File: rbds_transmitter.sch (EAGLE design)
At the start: 111 parts, among them IC1 MAX1551, IC2 TPS61030, IC3 MCP4812, IC4 OPA4743UA, IC5 OPA4743UA, IC6 MAX2606, Q1 P-Ch, Q2 P-CH, SW1 FSMSM, U3 ATMEGA328, X1 HD44780LCD-1602, Y1 16Mhz

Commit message: rebuilding filter systems
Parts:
- removed C13: 3.8nF, adafruit:C-USC1206
- removed C15, C16, C17, C20, C21, C22, C26, C27, C35, C36, C37: (no value), adafruit:C-USC1206
- removed IC4, IC5: OPA4743UA, linear:OPA4743UA
- removed R22, R23, R24, R28, R29, R30, R31, R32, R33, R34, R35, R37, R40, R41: (no value), adafruit:R-US_R1206
- removed R26, R27, R36: 100k, rcl:R-TRIMM4G/J
- added C33, C38, C39, C40, C41, C42, C43, C45, C46, C47, C48, C49, C50, C51, C52, C53, C54, C55, C56, C57: (no value), adafruit:C-USC1206
- added IC11, IC12: OPA4743UA, linear:OPA4743UA
- added R46, R47, R48, R49, R50, R52, R53, R54, R56, R57, R58, R61, R62, R63, R64, R65, R66, R68, R69, R70, R71: (no value), adafruit:R-US_R1206
- added R51, R55, R59, R67: 100k, rcl:R-TRIMM4G/J
- C11: value 10uF -> (none)
- C12: value 1.9nF -> (none)
- R16, R17: value 100k -> (none)
- R18, R19: value 1k -> 100k; device adafruit:R-US_R1206 -> rcl:R-TRIMM4G/J
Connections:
- removed net N$21: C27.2
- removed net N$25: C13.1, R18.1, R19.2
- removed net N$31: C12.1, IC4A.+IN, R19.1
- removed net N$32: C17.1, R26.S
- removed net N$34: C15.1, IC4D.+IN, R28.1
- removed net N$36: C16.1, R28.2, R29.1
- removed net N$37: C21.1, R36.S
- removed net N$38: C17.2, R29.2, R30.1, R31.2
- removed net N$40: C20.1, IC5A.+IN, R35.2
- removed net N$41: C22.1, R34.2, R35.1
- removed net N$43: C21.2, R32.2, R33.1, R34.1
- removed net N$44: C13.2, C35.1, IC4A.-IN, IC4A.OUT
- removed net N$45: C22.2, C36.1, IC5A.-IN, IC5A.OUT
- removed net N$47: C24.1, IC5C.+IN, R39.1
- removed net N$48: C37.2, R24.2
- removed net N$49: C11.1, R27.S
- removed net N$51: C26.2, R38.2, R40.1, R41.2
- removed net N$56: C36.2, R22.2
- removed net N$57: C35.2, R23.2
- new net FREQUENCY_OFFSET: R20.1
- new net N$59: C56.1, R65.1, R66.2
- new net N$60: C38.1, R46.1, R47.2
- new net N$61: C39.1, R47.1, R48.2
- new net N$62: C40.1, R48.1, R51.A
- new net N$63: C54.1, R67.A, R71.1
- new net N$64: IC11B.-IN, R51.S
- new net N$65: C41.1, IC11B.OUT, R51.E
- new net N$66: C53.1, IC12B.+IN, R49.1, R50.2
- new net N$67: C43.1, R52.1, R53.2
- new net N$68: C45.1, R53.1, R54.2
- new net N$69: C46.1, R54.1, R55.A
- new net N$70: IC11D.-IN, R55.S
- new net N$71: C47.1, IC11D.OUT, R55.E
- new net N$72: C49.1, R56.1, R57.2
- new net N$73: C50.1, R57.1, R58.2
- new net N$74: C51.1, R58.1, R59.A
- new net N$75: IC11C.-IN, R59.S
- new net N$76: C52.1, IC11C.OUT, R59.E
- new net N$77: IC11A.-IN, R67.S
- new net N$78: C41.2, R61.2
- new net N$79: C47.2, R62.2
- new net N$80: C52.2, R63.2
- new net N$81: C11.1, R61.1, R62.1, R63.1
- new net N$82: C25.1, IC11A.OUT, R67.E
- new net N$83: C33.1, R46.2, R68.1
- new net N$84: C42.1, R52.2, R69.1
- new net N$85: C48.1, R56.2, R70.1
- new net N$86: C57.1, R66.1, R71.2
- net +5V: now also IC11P.V+, IC12P.V+, R17.1, R39.1, R50.1; no longer IC4P.V+, IC5P.V+, R16.2, R31.1, R32.1, R41.1
- net AGND: now also IC11A.+IN, IC11B.+IN, IC11C.+IN, IC11D.+IN, IC12A.+IN, IC12B.-IN, IC12B.OUT, R19.A
- net BPSK: now also C23.1, IC12C.-IN, IC12C.OUT; no longer IC4C.-IN, IC4C.OUT, R15.2
- net CARRIER: now also R64.2; no longer C26.1
- net FREQUENCY: now also IC12D.-IN, IC12D.OUT; no longer IC5B.-IN, IC5B.OUT, R37.2
- net GND: now also C33.2, C38.2, C39.2, C40.2, C42.2, C43.2, C45.2, C46.2, C48.2, C49.2, C50.2, C51.2, C53.2, C54.2, C55.2, C56.2, C57.2, IC11P.V-, IC12P.V-, R16.2, R21.2, R38.2, R49.2, TR2.3; no longer C12.2, C15.2, C20.2, C24.2, IC4P.V-, IC5D.+IN, IC5P.V-, R17.1, R20.2, R26.A, R27.A, R30.2, R33.2, R36.A, R40.2, TR1.3
- net N$19: now also TR1.3; no longer TR2.5
- net N$22: now also IC12A.-IN, R18.S; no longer C11.2, R16.1, R17.2, R18.2
- net N$23: now also IC12A.OUT, R18.E, R19.E; no longer IC4B.-IN, R20.1, R21.2
- net N$26: now also C12.1, R19.S; no longer C27.1, IC4B.OUT, R21.1
- net N$28: now also IC12C.+IN; no longer IC4C.+IN
- net N$29: now also C12.2, R20.2, R21.1; no longer C16.2, C37.1, IC4D.-IN, IC4D.OUT
- net N$30: now also R15.2; no longer C25.1, IC5C.-IN, IC5C.OUT
- net N$42: now also C24.1, TR2.5; no longer C23.1, R38.1, R39.2
- net N$46: now also IC12D.+IN; no longer IC5B.+IN
- net N$5: now also C11.2, R16.1, R17.2, R18.A; no longer IC4B.+IN, R22.1, R23.1, R24.1, R37.1
- net N$55: now also C55.1, R64.1, R65.2; no longer IC5D.-IN, IC5D.OUT
- net PILOT: now also R69.2; no longer R36.E
- net RBDS: now also C24.2, R38.1, R39.2, R68.2; no longer R27.E, TR2.3
- net TONE: now also R70.2; no longer R26.E
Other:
- moved on the sheet: ANT1, ANT2, C1, C10, C11, C12, C14, C18, C19, C2, C23, C24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

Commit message: need to wire subsystems to mcu
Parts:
- removed SW1: FSMSM, alcoswitch:FSMSM
- C1: value 4.7uF -> 1nF
- C11, C12, C14, C28, C32, C41, C47, C52, C53, C9: value (none) -> 1uF
- C18, C29, C30, C8: value (none) -> 4.7uF
- C19, C34: value (none) -> 100pF
- C23, C24, C25: value (none) -> 10uF
- C33, C38, C39, C40: value (none) -> 1.34nF
- C42, C43, C45, C46: value (none) -> 4.188nF
- C48, C49, C50, C51: value (none) -> 3.06nF
- C54, C55, C56, C57: value (none) -> 1.396nF
- C7: value (none) -> 100uF; device adafruit:C-USC1206 -> adafruit:CPOL-US140CLH-1014
- L2: value (none) -> 485nH
- R11, R16, R17, R20, R21, R38, R39, R49, R50: value (none) -> 100k
- R44, R45: value (none) -> 10k
- R46, R47, R48, R52, R53, R54, R56, R57, R58, R64, R65, R66, R68, R69, R70, R71: value (none) -> 2k
- R61, R62, R63: value (none) -> 1k
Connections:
- removed net FREQUENCY_OFFSET: R20.1
- removed net N$29: C12.2, R20.2, R21.1
- removed net N$58: R42.1
- removed net RST: C1.2
- new net SIGNAL: C12.2, R20.2, R21.1, R42.1
- net !ISP-RST: no longer C1.1, SW1.S
- net +5V: now also C7.+; no longer C7.1
- net FREQUENCY: now also R20.1
- net GND: now also C1.2, C7.-; no longer C7.2, SW1.P
- net N$27: now also C1.1
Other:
- moved on the sheet: ANT1, ANT2, C1, C10, C11, C12, C14, C18, C19, C2, C23, C24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

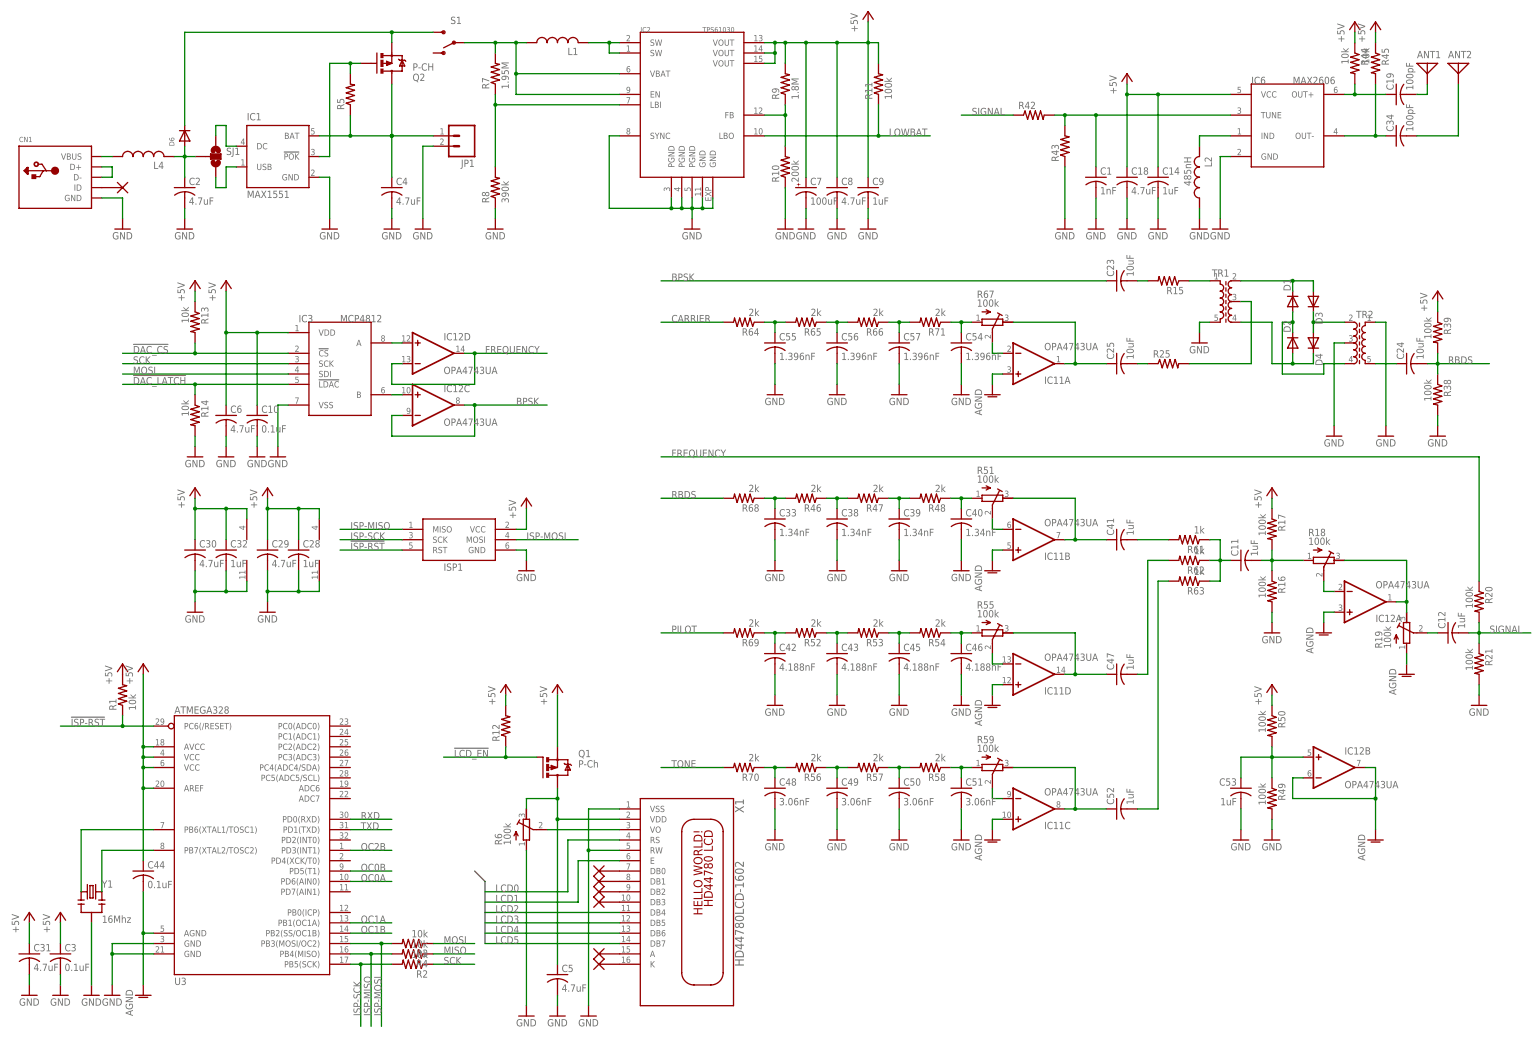
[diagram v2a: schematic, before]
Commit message: finished prelim layout
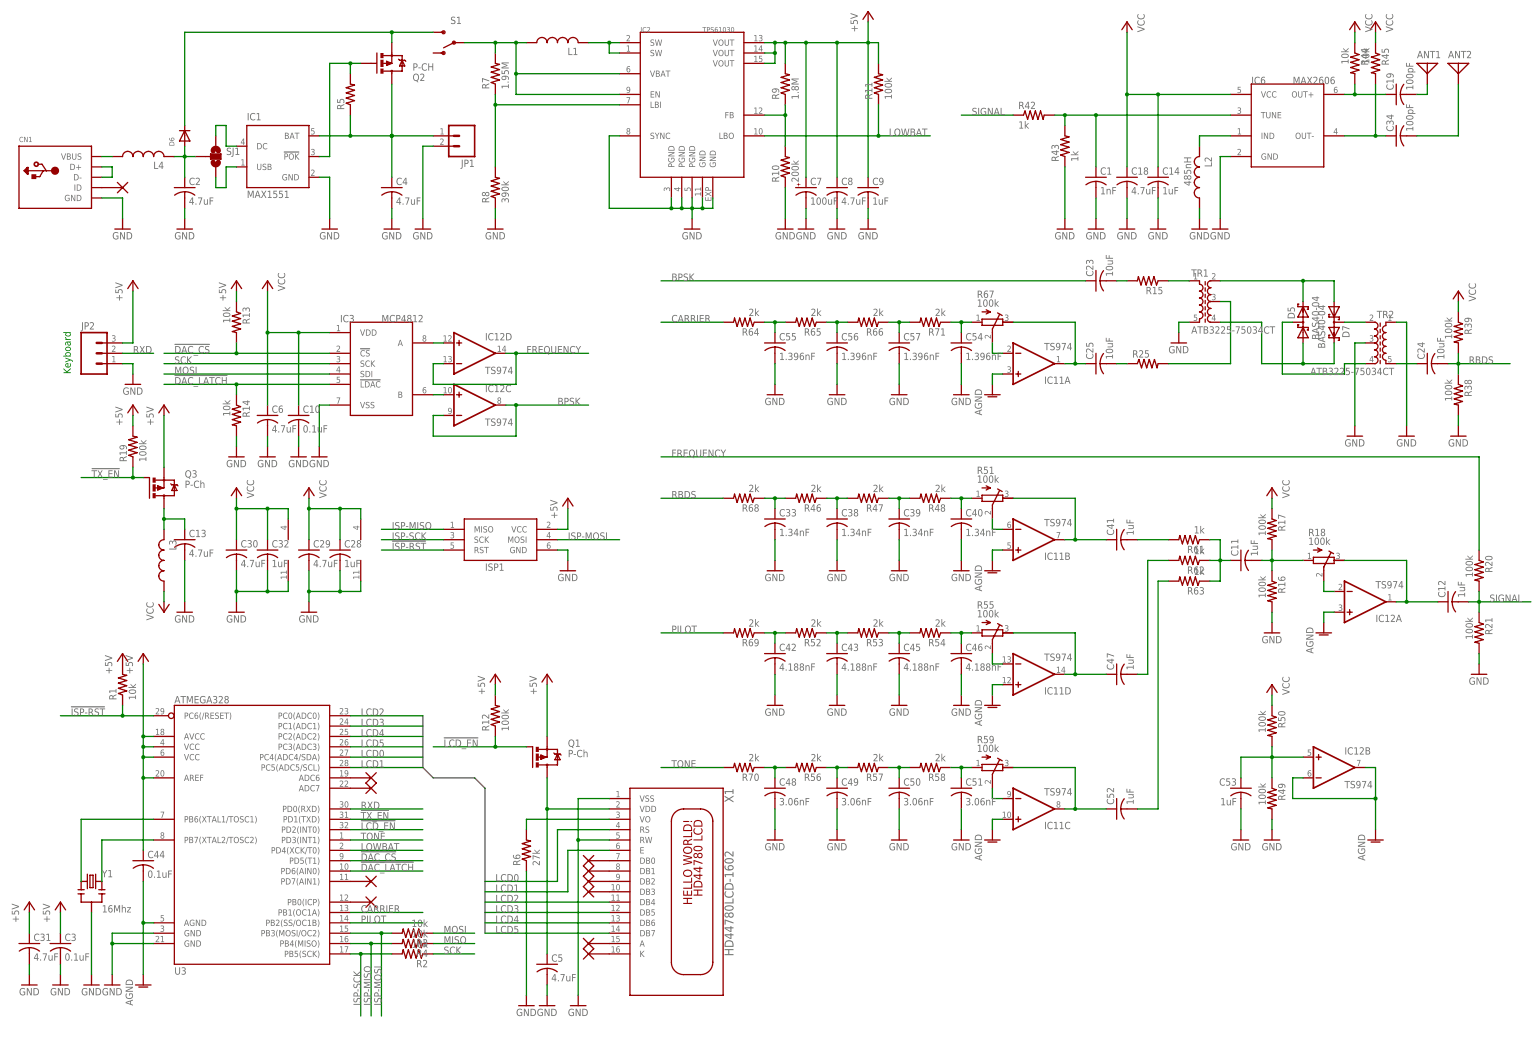
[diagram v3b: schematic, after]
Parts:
- removed D1, D2, D3, D4: (no value), dp_devices:DIODE-SOD-123
- added C13: 4.7uF, adafruit:C-USC1206
- added D5, D7: BAS40-04, diode:BAS40-04
- added JP2: (no value), sparkfun:M03PTH
- added L3: (no value), resistor:L-USL1812
- added Q3: P-Ch, transistor-power:IRLML5203
- IC11, IC12: value OPA4743UA -> TS974
- R12: value (none) -> 100k
- R19: device rcl:R-TRIMM4G/J -> adafruit:R-US_R1206
- R42, R43: value (none) -> 1k
- R6: value 100k -> 27k; device rcl:R-TRIMM4G/J -> adafruit:R-US_R1206
- TR1, TR2: value (none) -> ATB3225-75034CT
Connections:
- removed net N$26: C12.1, R19.S
- removed net OC0A: U3.PD6(AIN0)
- removed net OC0B: U3.PD5(T1)
- removed net OC1A: U3.PB1(OC1A)
- removed net OC1B: U3.PB2(SS/OC1B)
- removed net OC2B: U3.PD3(INT1)
- removed net TXD: U3.PD1(TXD)
- new net !TX_EN: Q3.G, R19.1, U3.PD1(TXD)
- new net N$21: C13.1, L3.2, Q3.D
- new net VCC: C10.1, C14.1, C18.1, C28.1, C29.1, C30.1, C32.1, C6.1, IC11P.V+, IC12P.V+, IC3.VDD, IC6.VCC, L3.1, R17.1, R39.1, R44.1, R45.1, R50.1
- net !DAC_CS: now also U3.PD5(T1)
- net !DAC_LATCH: now also U3.PD6(AIN0)
- net !LCD_EN: now also U3.PD2(INT0)
- net +5V: now also JP2.3, Q3.S, R19.2; no longer C10.1, C14.1, C18.1, C28.1, C29.1, C30.1, C32.1, C6.1, IC11P.V+, IC12P.V+, IC3.VDD, IC6.VCC, R17.1, R39.1, R44.1, R45.1, R50.1
- net AGND: no longer R19.A
- net CARRIER: now also U3.PB1(OC1A)
- net GND: now also C13.2, JP2.1, R6.1; no longer R6.A
- net LCD0: now also U3.PC4(ADC4/SDA)
- net LCD1: now also U3.PC5(ADC5/SCL)
- net LCD2: now also U3.PC0(ADC0)
- net LCD3: now also U3.PC1(ADC1)
- net LCD4: now also U3.PC2(ADC2)
- net LCD5: now also U3.PC3(ADC3)
- net LOWBAT: now also U3.PD4(XCK/T0)
- net N$14: now also D7.C1A2; no longer D3.C, D4.A
- net N$16: now also D5.C2, D7.A1; no longer D1.C, D3.A
- net N$18: now also D5.A1, D7.C2; no longer D2.A, D4.C
- net N$23: now also C12.1; no longer R19.E
- net N$3: now also D5.C1A2; no longer D1.A, D2.C
- net N$9: now also R6.2; no longer R6.S
- net PILOT: now also U3.PB2(SS/OC1B)
- net RXD: now also JP2.2
- net TONE: now also U3.PD3(INT1)
- net VDD: no longer R6.E
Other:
- note added: "Keyboard"
- moved on the sheet: C10, C12, C23, C24, C25, C28, C29, C3, C30, C31, C32, C44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

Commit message: finsihed
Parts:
- removed C47, C52, C53: 1uF, adafruit:C-USC1206
- removed C50, C51: 3.06nF, adafruit:C-USC1206
- removed C54, C55, C56, C57: 1.396nF, adafruit:C-USC1206
- removed IC11, IC12: TS974, linear:OPA4743UA
- removed R54, R56, R57, R58: 2k, adafruit:R-US_R1206
- removed R55, R59, R67: 100k, rcl:R-TRIMM4G/J
- removed R61, R62: 1k, adafruit:R-US_R1206
- added C15: 10uF, adafruit:C-USC1206
- added C16: 100pF, adafruit:C-USC1206
- added C17, C20, C21, C22, C26, C27: 4.7uF, adafruit:C-USC1206
- added C35: 1.34nF, adafruit:C-USC1206
- added IC4: MAX2606, maxim:MAX2606
- added IC5: TPS61030, texas:TPS61030
- added JP10, JP3, JP4, JP5, JP6, JP7, JP8, JP9: M01PTH, sparkfun:M01PTH
- added JP11: (no value), sparkfun:M023.5MM
- added R22, R23, R24, R40, R41: 100k, adafruit:R-US_R1206
- added R26, R27, R28: 10k, adafruit:R-US_R1206
- added R37: 1.8M, adafruit:R-US_R1206
- C10, C3: value 0.1uF -> 1uF
- C12: value 1uF -> 0.1uF
- C13: value 4.7uF -> 10uF
- C14: value 1uF -> 10uF
- C18: value 4.7uF -> 0.1uF
- C19: value 100pF -> 4.7uF
- C2, C4, C5, C6, C8: value 4.7uF -> 1uF
- C23: value 10uF -> 0.1uF
- C24, C25: value 10uF -> 4.7uF
- C28: value 1uF -> 4.7uF
- C29, C30, C31: value 4.7uF -> 1.396nF
- C32: value 1uF -> 1.34nF
- C34: value 100pF -> 1.34nF
- C38, C39: value 1.34nF -> 3.06nF
- C40: value 1.34nF -> 100pF
- C41: value 1uF -> 4.188nF
- C44: value 0.1uF -> 4.188nF
- C45: value 4.188nF -> 1.396nF
- C46: value 4.188nF -> 100uF; device adafruit:C-USC1206 -> adafruit:CPOL-US140CLH-1014
- C7: value 100uF -> 1uF; device adafruit:CPOL-US140CLH-1014 -> adafruit:C-USC1206
- IC1: value MAX1551 -> TS974; device maxim:MAX1551 -> linear:OPA4743UA
- IC2: value TPS61030 -> TS974; device texas:TPS61030 -> linear:OPA4743UA
- IC3: value MCP4812 -> MAX1551; device microchip:MCP4812 -> maxim:MAX1551
- IC6: value MAX2606 -> MCP4812; device maxim:MAX2606 -> microchip:MCP4812
- JP1: device sparkfun:M02-JST-2MM-SMT -> sparkfun:M03PTH
- JP2: device sparkfun:M03PTH -> sparkfun:M02-JST-2MM-SMT
- L2: value 485nH -> (none)
- L4: value (none) -> 485nH
- Q1: value P-Ch -> P-CH; device transistor-power:IRLML5203 -> sparkfun:MOSFET-PCHANNELSMD
- Q2: value P-CH -> P-Ch; device sparkfun:MOSFET-PCHANNELSMD -> transistor-power:IRLML5203
- R1: value 10k -> 332
- R10: value 200k -> 2k
- R11, R12, R16, R17: value 100k -> 2k
- R13, R14: value 10k -> 2k
- R15: value (none) -> 2k
- R18: value 100k -> 1k; device rcl:R-TRIMM4G/J -> adafruit:R-US_R1206
- R19: value 100k -> 1k
- R20: value 100k -> (none)
- R21: value 100k -> 200
- R25: value (none) -> 10k
- R38: value 100k -> 390k
- R39: value 100k -> 200k
- R42, R43: value 1k -> 100k
- R44, R45: value 10k -> 100k
- R46, R47: value 2k -> 100k
- R48: value 2k -> 1.95M
- R49, R50: device adafruit:R-US_R1206 -> rcl:R-TRIMM4G/J
- R5: value (none) -> 200
- R52, R53: value 2k -> 100k; device adafruit:R-US_R1206 -> rcl:R-TRIMM4G/J
- R6: value 27k -> 10k
- R7: value 1.95M -> 10k
- R8: value 390k -> 10k
- R9: value 1.8M -> 2k
- renumbered C48 to C36, C49 to C37, D5 to D2, D6 to D1, D7 to D3, R63 to R29, R64 to R30, R65 to R31, R66 to R32, R68 to R33, R69 to R34, R70 to R35, R71 to R36, S1 to SW1, U3 to U1
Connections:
- removed net N$27: C1.1, IC6.TUNE, R42.2, R43.2
- removed net N$30: C23.2, R15.2
- removed net N$53: C25.2, R25.1
- new net N$25: C13.1, R5.1
- new net N$26: C15.1, R21.2
- net !DAC_CS: now also IC6.!CS, R2.2; no longer IC3.!CS, R13.2
- net !DAC_LATCH: now also IC6.!LDAC, R3.1; no longer IC3.!LDAC, R14.1
- net !ISP-RST: now also R25.1; no longer R1.1
- net !LCD_EN: now also Q2.G, R41.1; no longer Q1.G, R12.1
- net !TX_EN: now also R44.1; no longer R19.1
- net +5V: now also C12.1, C18.1, C2.1, C22.1, C28.1, C46.+, IC5.VOUT@0, IC5.VOUT@1, IC5.VOUT@2, JP1.3, JP11.2, Q2.S, R2.1, R25.2, R37.2, R40.2, R41.2, R44.2; no longer C3.1, C31.1, C44.1, C7.+, C8.1, C9.1, IC2.VOUT@0, IC2.VOUT@1, IC2.VOUT@2, JP2.3, Q1.S, R1.2, R11.2, R12.2, R13.1, R19.2, R9.2
- net AGND: now also C12.2, IC1A.+IN, IC1B.+IN, IC1C.+IN, IC1D.+IN, IC2A.+IN, IC2B.-IN, IC2B.OUT; no longer C44.2, IC11A.+IN, IC11B.+IN, IC11C.+IN, IC11D.+IN, IC12A.+IN, IC12B.-IN, IC12B.OUT
- net BPSK: now also IC2C.-IN, IC2C.OUT, JP4.1, R5.2; no longer C23.1, IC12C.-IN, IC12C.OUT
- net FREQUENCY: now also IC2D.-IN, IC2D.OUT, JP3.1, R45.1; no longer IC12D.-IN, IC12D.OUT, R20.1
- net GND: now also C11.2, C17.2, C19.2, C20.2, C21.2, C22.2, C23.2, C24.2, C25.2, C26.2, C27.2, C34.2, C35.2, C41.2, C44.2, C46.-, C7.2, IC1P.V-, IC2P.V-, IC3.GND, IC4.GND, IC5.GND@0, IC5.GND@1, IC5.PGND@0, IC5.PGND@1, IC5.PGND@2, IC5.SYNC, IC6.VSS, JP1.1, JP11.1, JP2.2, L4.1, R1.1, R23.2, R3.2, R38.1, R39.1, R4.1, R42.2, R46.2, R47.2, TR1.1, TR1.3, TR2.5; no longer C10.2, C13.2, C14.2, C3.2, C4.2, C40.2, C46.2, C50.2, C51.2, C53.2, C54.2, C55.2, C56.2, C57.2, C7.-, C8.2, C9.2, IC1.GND, IC11P.V-, IC12P.V-, IC2.GND@0, IC2.GND@1, IC2.PGND@0, IC2.PGND@1, IC2.PGND@2, IC2.SYNC, IC3.VSS, IC6.GND, JP1.2, JP2.1, L2.1, R10.1, R14.2, R16.2, R21.2, R38.2, R43.1, R49.2, R6.1, R8.1, TR1.5, TR2.1, TR2.3
- net ISP-MISO: now also R28.2; no longer R4.2
- net ISP-MOSI: now also R27.2; no longer R3.2
- net ISP-SCK: now also R26.2; no longer R2.2
- net LOWBAT: now also IC5.LBO, R40.1; no longer IC2.LBO, R11.1
- net MISO: now also R28.1; no longer R4.1
- net MOSI: now also IC6.SDI, R27.1; no longer IC3.SDI, R3.1
- net N$1: now also C17.1, L3.2; no longer C2.1, L4.2
- net N$10: now also IC3.!POK, Q1.G, R20.2; no longer IC1.!POK, Q2.G, R5.2
- net N$11: now also C19.1, IC3.BAT, JP2.1, Q1.D, R20.1; no longer C4.1, IC1.BAT, JP1.1, Q2.D, R5.1
- net N$12: now also IC5.SW@0, IC5.SW@1; no longer IC2.SW@0, IC2.SW@1
- net N$14: now also TR1.2; no longer TR2.2
- net N$15: now also IC5.LBI, R38.2, R48.1; no longer IC2.LBI, R7.1, R8.2
- net N$16: now also TR2.2; no longer TR1.2
- net N$17: now also IC5.FB, R37.1, R39.2; no longer IC2.FB, R10.2, R9.1
- net N$18: now also TR2.4; no longer TR1.4
- net N$19: now also C15.2, TR2.3; no longer R25.2, TR1.3
- net N$20: now also C13.2, TR2.1; no longer R15.1, TR1.1
- net N$21: now also C24.1, L2.2; no longer C13.1, L3.2
- net N$22: now also IC2A.-IN, R53.S; no longer IC12A.-IN, R18.S
- net N$23: now also C4.1, IC2A.OUT, R53.E; no longer C12.1, IC12A.OUT, R18.E
- net N$24: now also IC4.IND, L4.2; no longer IC6.IND, L2.2
- net N$28: now also IC2C.+IN, IC6.B; no longer IC12C.+IN, IC3.B
- net N$3: now also TR1.4; no longer TR2.4
- net N$33: now also C40.1, IC4.OUT+, R7.2; no longer C19.1, IC6.OUT+, R44.2
- net N$35: now also C16.1, IC4.OUT-, R8.2; no longer C34.1, IC6.OUT-, R45.2
- net N$39: now also C40.2; no longer C19.2
- net N$42: now also C14.1, TR1.5; no longer C24.1, TR2.5
- net N$46: now also IC2D.+IN, IC6.A, R4.2, R6.1; no longer IC12D.+IN, IC3.A
- net N$5: now also C3.2, R42.1, R43.2, R53.A; no longer C11.2, R16.1, R17.2, R18.A
- net N$50: now also IC5.EN, IC5.VBAT, R48.2; no longer IC2.EN, IC2.VBAT, R7.2
- net N$52: now also C16.2; no longer C34.2
- net N$54: now also L3.1; no longer L4.1
- net N$55: now also C29.1; no longer C55.1
- net N$59: now also C30.1; no longer C56.1
- net N$6: now also Q1.S; no longer Q2.S
- net N$60: now also C33.1, R10.2, R9.1; no longer C38.1, R46.1, R47.2
- net N$61: now also C34.1, R10.1, R11.2; no longer C39.1, R47.1, R48.2
- net N$62: now also C35.1, R11.1, R49.A; no longer C40.1, R48.1, R51.A
- net N$63: now also C45.1, R52.A; no longer C54.1, R67.A
- net N$64: now also IC1B.-IN, R49.S; no longer IC11B.-IN, R51.S
- net N$65: now also C8.1, IC1B.OUT, JP6.1, R49.E; no longer C41.1, IC11B.OUT, R51.E
- net N$66: now also C11.1, IC2B.+IN, R23.1, R24.2; no longer C53.1, IC12B.+IN, R49.1, R50.2
- net N$67: now also C42.1, R12.1, R13.2; no longer C43.1, R52.1, R53.2
- net N$68: now also C43.1, R13.1, R14.2; no longer C45.1, R53.1, R54.2
- net N$69: now also C44.1, R14.1, R50.A; no longer C46.1, R54.1, R55.A
- net N$7: now also IC3.USB; no longer IC1.USB
- net N$70: now also IC1D.-IN, R50.S; no longer IC11D.-IN, R55.S
- net N$71: now also C9.1, IC1D.OUT, JP7.1, R50.E; no longer C47.1, IC11D.OUT, R55.E
- net N$72: now also R15.1, R16.2; no longer R56.1, R57.2
- net N$73: now also C38.1, R16.1, R17.2; no longer C50.1, R57.1, R58.2
- net N$74: now also C39.1, R17.1, R51.A; no longer C51.1, R58.1, R59.A
- net N$75: now also IC1C.-IN, R51.S; no longer IC11C.-IN, R59.S
- net N$76: now also C10.1, IC1C.OUT, JP8.1, R51.E; no longer C52.1, IC11C.OUT, R59.E
- net N$77: now also IC1A.-IN, R52.S; no longer IC11A.-IN, R67.S
- net N$78: now also C8.2, R18.2; no longer C41.2, R61.2
- net N$79: now also C9.2, R19.2; no longer C47.2, R62.2
- net N$8: now also IC3.DC; no longer IC1.DC
- net N$80: now also C10.2; no longer C52.2
- net N$81: now also C3.1, R18.1, R19.1; no longer C11.1, R61.1, R62.1
- net N$82: now also IC1A.OUT, JP5.1, R21.1, R52.E; no longer C25.1, IC11A.OUT, R67.E
- net N$83: now also C32.1, R9.2; no longer C33.1, R46.2
- net N$84: now also C41.1, R12.2; no longer C42.1, R52.2
- net N$85: now also R15.2; no longer R56.2
- net N$86: now also C31.1; no longer C57.1
- net N$9: now also R1.2; no longer R6.2
- net RBDS: now also C14.2, JP10.1, R22.2, R47.1; no longer C24.2, R38.1, R39.2
- net RXD: now also JP1.2; no longer JP2.2
- net SCK: now also IC6.SCK, R26.1; no longer IC3.SCK, R2.1
- net SIGNAL: now also C1.1, C4.2, IC4.TUNE, JP9.1, R45.2, R46.1; no longer C12.2, R20.2, R21.1, R42.1
- net VCC: now also C21.1, C23.1, C25.1, C26.1, C27.1, C5.1, C7.1, IC1P.V+, IC2P.V+, IC4.VCC, IC6.VDD, L2.1, R22.1, R24.1, R43.1, R6.2, R7.1, R8.1; no longer C10.1, C14.1, C18.1, C28.1, C29.1, C30.1, C32.1, IC11P.V+, IC12P.V+, IC3.VDD, IC6.VCC, L3.1, R17.1, R39.1, R44.1, R45.1, R50.1
- net VDD: now also C20.1, Q2.D; no longer C5.1, Q1.D
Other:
- note added: "C46"
- note added: "D3"
- note added: "IC6"
- note added: "JP10"
- note added: "L4"
- note added: "LDU"
- note added: "Q3"
- note added: "R53"
- note added: "SW1"
- note added: "T2"
- note added: "Y1"
- moved on the sheet: C1, C10, C11, C12, C13, C14, C18, C19, C2, C23, C24, C25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
